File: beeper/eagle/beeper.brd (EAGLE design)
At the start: 29.2 x 39.8 mm, 30 parts, among them J4 ICSP, T1 MMBT3904, U1 ATA6631, U2 ATMEGA328P, X1 16MHz

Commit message: More beeper library cleanup.
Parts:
- C4: device rcl:C0805 -> beeper:C0805
- R3: device rcl:R0805 -> beeper:R0805
- T1: device transistor:SOT23-BEC -> beeper:SOT23-BEC
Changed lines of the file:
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@@
 <attribute name="NAME" x="25.4" y="26.4922" size="1.016" layer="25" ratio="10" rot="R270"/>
 </element>
-<element name="R3" library="rcl" package="R0805" value="3.3K" x="18.6182" y="13.5636" smashed="yes" rot="R180">
+<element name="R3" library="beeper" package="R0805" value="3.3K" x="18.6182" y="13.5636" smashed="yes" rot="R180">
 <attribute name="NAME" x="16.7894" y="13.208" size="1.016" layer="25" rot="R180"/>
 </element>
-<element name="T1" library="transistor" package="SOT23-BEC" value="MMBT3904" x="16.383" y="6.7564" smashed="yes" rot="R90">
+<element name="T1" library="beeper" package="SOT23-BEC" value="MMBT3904" x="16.383" y="6.7564" smashed="yes" rot="R90">
 <attribute name="NAME" x="14.8336" y="8.2804" size="1.016" layer="25" rot="R180"/>
 </element>
@@
 <attribute name="NAME" x="11.6238" y="14.1028" size="1.016" layer="25" rot="R90"/>
 </element>
-<element name="C4" library="rcl" package="C0805" value="0.1uF" x="14.8082" y="21.2344" smashed="yes" rot="R270">
+<element name="C4" library="beeper" package="C0805" value="0.1uF" x="14.8082" y="21.2344" smashed="yes" rot="R270">
 <attribute name="NAME" x="12.8524" y="21.4884" size="1.016" layer="25" rot="R270"/>
 </element>

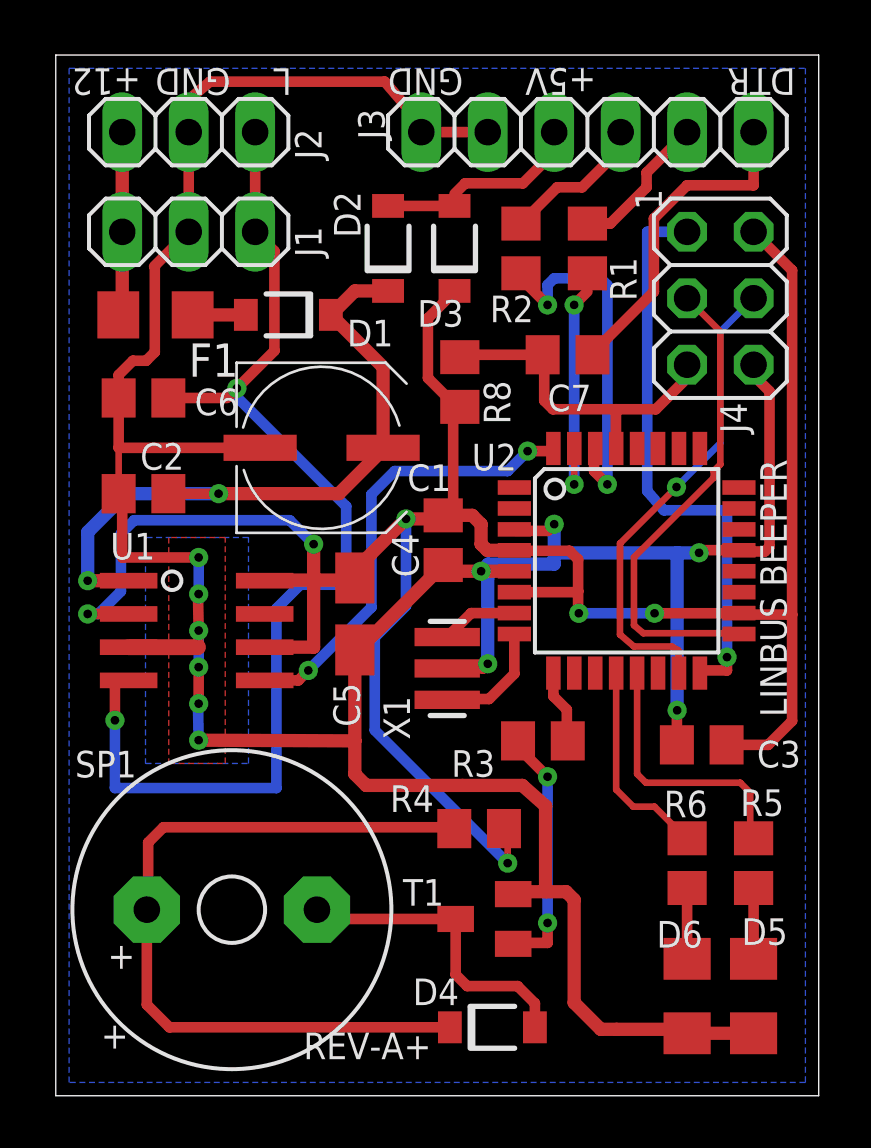
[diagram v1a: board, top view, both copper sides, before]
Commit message: Updated beeper board and schematic for Rev B.
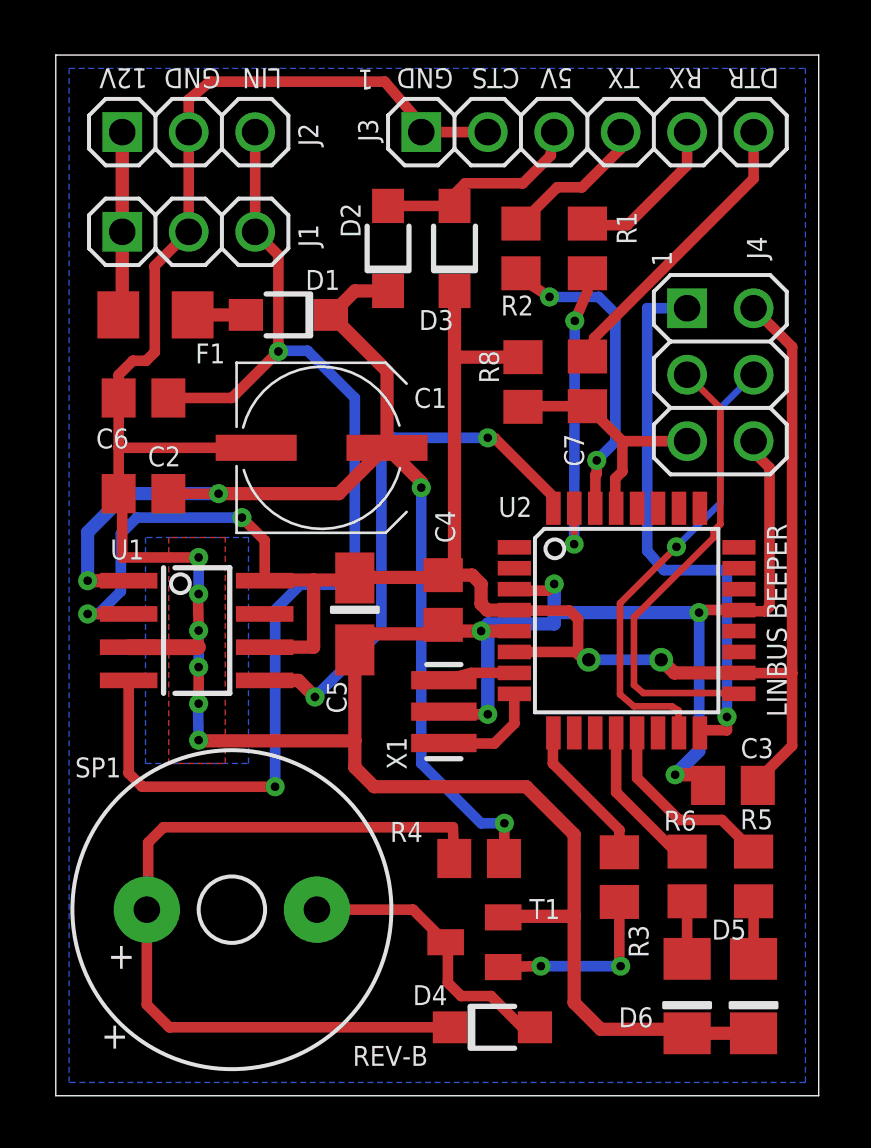
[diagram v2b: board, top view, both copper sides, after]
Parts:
- D5, D6: device beeper:1206 -> beeper:1206-LED
- R1, R2, R8: value 10k -> 10K
- R3, R5, R6: value 3.3K -> 3K3
- R4: value 0 -> 200R
- moved R3 5.97 mm to (21.5, 8.36), turned to 270 degrees
- moved J4 2.92 mm to (25.4, 27.6)
- moved R8 2.41 mm to (17.9, 27.3), turned to 90 degrees
- moved C4 2.29 mm to (14.8, 18.9)
- moved U2 2.29 mm to (21.8, 18.2)
- moved C3 1.96 mm to (25.9, 11.9)
- moved X1 1.66 mm to (14.8, 14.7)
- moved C7 1.27 mm to (20.3, 27.3), turned to 270 degrees
- moved R4 1.14 mm to (16.2, 9.07)
- moved T1 0.97 mm to (16.0, 5.87)
- moved R5 0.51 mm to (26.7, 8.38)
- moved R6 0.51 mm to (24.1, 8.38)
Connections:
- net +12V: now also R4.2
- net +5V: no longer R4.2
- net DTR: now also J3.6; no longer J3.1
- net GND: now also D5.C, D6.C, J3.1, J3.2; no longer D5.2, D6.2, J3.5, J3.6
- net N$3: now also D6.A; no longer D6.1
- net N$4: now also D5.A; no longer D5.1
- net RXI: now also J3.5; no longer J3.2
- net S-5V: now also J3.3; no longer J3.4
- net TXO: now also J3.4; no longer J3.3
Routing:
- net +5V: track 97.4 -> 77.8 mm, vias 6 -> 4
- net +12V: track 26.5 -> 44.7 mm, vias 2 -> 4
- net LIN_RX: track 17.2 -> 20.8 mm
- net RESET: track 13.1 -> 9.54 mm
- net ERROR_LED: track 10.3 -> 7.34 mm
- net BUZZER: track 2.82 -> 5.62 mm
- net N$19: track 9.52 -> 6.96 mm
- net SER_TX: track 9.65 -> 11.8 mm
- net FRAME_LED: track 7.93 -> 5.92 mm
- net SER_RX: track 14.1 -> 12.1 mm
- net DTR: track 12.5 -> 11.2 mm
- net N$30: track 30.1 -> 31.2 mm
- net N$31: track 12.0 -> 11.1 mm
- net XTAL2: track 4.94 -> 4.27 mm
- net MOSI: track 18.3 -> 17.7 mm
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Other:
- board text added: "12V"
- board text added: "5V"
- board text added: "CTS"
- board text added: "LIN"
- board text added: "REV-B"
- board text added: "RX"
- board text added: "TX"
- board text removed: "+12"
- board text removed: "+5V"
- board text removed: "L"
- board text removed: "REV-A+"

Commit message: Changed the beeper schematic to use the full atmega328p symbol. No Semantic change.
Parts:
- U2: value ATMEGA328P -> ATMEGA328
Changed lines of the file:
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@@
 <attribute name="NAME" x="10.8646" y="31.5628" size="0.762" layer="25" rot="R180"/>
 </element>
-<element name="U2" library="beeper" package="TQFP32-08" value="ATMEGA328P" x="21.8186" y="18.161" smashed="yes">
+<element name="U2" library="beeper" package="TQFP32-08" value="ATMEGA328" x="21.8186" y="18.161" smashed="yes">
 <attribute name="NAME" x="16.9164" y="22.1234" size="0.762" layer="25"/>
 </element>

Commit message: Completed the beeper schema cleanup. Added NC and debug signal ndicators.
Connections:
- net MISO renamed MISO/LIN_DATA
- net MOSI renamed MOSI/LIN_ERROR
- new net GP_DEBUG: U2.10
- new net LIN_BREAK: U2.23
- new net LIN_ISR: U2.26
- new net LIN_TICK: U2.1
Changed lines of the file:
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@@
 <wire x1="15.24" y1="34.4678" x2="15.24" y2="34.01" width="0.254" layer="1"/>
 </signal>
-<signal name="MOSI">
+<signal name="MOSI/LIN_ERROR">
 <contactref element="J4" pad="4"/>
 <contactref element="U2" pad="15"/>
@@
 <wire x1="25.4" y1="26.289" x2="26.67" y2="27.559" width="0.254" layer="16"/>
 </signal>
-<signal name="MISO">
+<signal name="MISO/LIN_DATA">
 <contactref element="J4" pad="1"/>
 <contactref element="U2" pad="16"/>
@@
 <signal name="N$1">
 </signal>
+<signal name="GP_DEBUG">
+<contactref element="U2" pad="10"/>
+</signal>
+<signal name="LIN_TICK">
+<contactref element="U2" pad="1"/>
+</signal>
+<signal name="LIN_BREAK">
+<contactref element="U2" pad="23"/>
+</signal>
+<signal name="LIN_ISR">
+<contactref element="U2" pad="26"/>
+</signal>
 </signals>

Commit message: Tweaked the layout. Should be ready for rev B.
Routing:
- net N$30: track 31.2 -> 30.6 mm
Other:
- board text added: "FEB/2014"
- board text added: "ICSP"
- board text added: "LINBUS BEEPER - REV B"
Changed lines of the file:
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@@
 <layer number="28" name="bValues" color="7" fill="1" visible="yes" active="yes"/>
 <layer number="29" name="tStop" color="7" fill="3" visible="no" active="yes"/>
-<layer number="30" name="bStop" color="7" fill="6" visible="no" active="yes"/>
+<layer number="30" name="bStop" color="7" fill="6" visible="yes" active="yes"/>
 <layer number="31" name="tCream" color="7" fill="4" visible="no" active="yes"/>
 <layer number="32" name="bCream" color="7" fill="5" visible="no" active="yes"/>
@@
 <wire x1="29.1592" y1="39.7764" x2="0" y2="39.7764" width="0" layer="20"/>
 <wire x1="0" y1="39.7764" x2="0" y2="0" width="0" layer="20"/>
-<text x="27.94" y="14.478" size="0.762" layer="21" rot="R90">LINBUS BEEPER</text>
-<text x="14.224" y="1.905" size="0.762" layer="21" rot="R180">REV-B</text>
+<text x="28.194" y="13.843" size="0.762" layer="21" rot="R90">LINBUS BEEPER</text>
+<text x="14.351" y="1.651" size="0.762" layer="21" rot="R180">REV-B</text>
 <text x="3.5052" y="39.2684" size="0.762" layer="21" rot="SR180">12V</text>
 <text x="6.2992" y="39.2684" size="0.762" layer="21" rot="SR180">GND</text>
@@
 <text x="15.1892" y="39.2684" size="0.762" layer="21" rot="SR180">GND</text>
 <text x="19.7612" y="39.2684" size="0.762" layer="21" rot="SR180">5V</text>
-<text x="23.5458" y="31.6992" size="0.762" layer="21" rot="SR90">1</text>
+<text x="23.7998" y="31.8262" size="0.762" layer="21" rot="SR90">1</text>
 <text x="27.6352" y="39.2684" size="0.762" layer="21" rot="SR180">DTR</text>
 <text x="1.7272" y="1.8034" size="1.016" layer="21" rot="SR0">+</text>
@@
 <text x="22.3012" y="39.2684" size="0.762" layer="21" rot="SR180">TX</text>
 <text x="17.7292" y="39.2684" size="0.762" layer="21" rot="SR180">CTS</text>
-<text x="12.1412" y="39.2176" size="0.762" layer="21" rot="SR180">1</text>
+<text x="12.5222" y="35.9156" size="0.762" layer="21" rot="SR180">1</text>
+<text x="27.94" y="2.159" size="1.016" layer="30" font="vector" ratio="15" rot="MR180" align="bottom-right">LINBUS BEEPER - REV B</text>
+<text x="25.527" y="31.877" size="0.762" layer="21" rot="R90">ICSP</text>
+<text x="16.637" y="11.43" size="0.762" layer="21">FEB/2014</text>
 </plain>
 <attributes>
@@
 <param name="mlMinCreamFrame" value="0mil"/>
 <param name="mlMaxCreamFrame" value="0mil"/>
-<param name="mlViaStopLimit" value="13mil"/>
+<param name="mlViaStopLimit" value="20mil"/>
 <param name="srRoundness" value="0"/>
 <param name="srMinRoundness" value="0mil"/>
@@
 </element>
 <element name="J1" library="beeper" package="1X03" value="" x="5.08" y="33.02" smashed="yes">
-<attribute name="NAME" x="10.033" y="32.4358" size="0.762" layer="25" ratio="10" rot="R90"/>
+<attribute name="NAME" x="10.16" y="33.4518" size="0.762" layer="25" ratio="10" rot="SR180"/>
 <attribute name="VALUE" x="1.27" y="29.845" size="1.27" layer="27"/>
 </element>
 <element name="C3" library="beeper" package="C0805" value="0.1uF" x="25.8826" y="11.8618" smashed="yes" rot="R180">
-<attribute name="NAME" x="27.432" y="13.6652" size="0.762" layer="25" rot="R180"/>
+<attribute name="NAME" x="26.543" y="13.5382" size="0.762" layer="25" rot="R180"/>
 </element>
 <element name="C7" library="beeper" package="C0805" value="0.1uF" x="20.32" y="27.305" smashed="yes" rot="R270">
-<attribute name="NAME" x="19.431" y="25.2984" size="0.762" layer="25" rot="R270"/>
+<attribute name="NAME" x="21.336" y="27.8384" size="0.762" layer="25" rot="R270"/>
 </element>
 <element name="R1" library="beeper" package="R0805" value="10K" x="20.32" y="32.385" smashed="yes" rot="R90">
@@
 </element>
 <element name="J4" library="beeper" package="2X03" value="ICSP" x="25.4" y="27.559" smashed="yes" rot="R270">
-<attribute name="NAME" x="26.416" y="32.8422" size="0.762" layer="25" ratio="10" rot="R270"/>
+<attribute name="NAME" x="27.051" y="31.9532" size="0.762" layer="25" ratio="10" rot="R90"/>
 </element>
 <element name="R3" library="beeper" package="R0805" value="3K3" x="21.5392" y="8.3566" smashed="yes" rot="R270">
-<attribute name="NAME" x="21.8948" y="6.5278" size="0.762" layer="25" rot="R270"/>
+<attribute name="NAME" x="19.2278" y="8.6868" size="0.762" layer="25"/>
 </element>
 <element name="T1" library="beeper" package="SOT23-BEC" value="MMBT3904" x="16.002" y="5.8674" smashed="yes" rot="R90">
-<attribute name="NAME" x="19.2786" y="7.5184" size="0.762" layer="25" rot="R180"/>
+<attribute name="NAME" x="19.2786" y="6.5024" size="0.762" layer="25" rot="R180"/>
 </element>
 <element name="R4" library="beeper" package="R0805" value="200R" x="16.1798" y="9.0678" smashed="yes">
-<attribute name="NAME" x="12.7762" y="9.7028" size="0.762" layer="25"/>
+<attribute name="NAME" x="14.8082" y="10.2108" size="0.762" layer="25"/>
 </element>
 <element name="R8" library="beeper" package="R0805" value="10K" x="17.8562" y="27.2796" smashed="yes" rot="R90">
-<attribute name="NAME" x="16.9418" y="27.2288" size="0.762" layer="25" rot="R90"/>
+<attribute name="NAME" x="16.8148" y="26.4668" size="0.762" layer="25" rot="R90"/>
 </element>
 <element name="U1" library="beeper" package="SO-08" value="ATA6631" x="5.3848" y="17.78" smashed="yes" rot="R270">
@@
 </element>
 <element name="J3" library="beeper" package="1X06" value="" x="20.32" y="36.83" smashed="yes" rot="R180">
-<attribute name="NAME" x="11.557" y="37.338" size="0.762" layer="25" ratio="10" rot="R270"/>
+<attribute name="NAME" x="12.319" y="37.211" size="0.762" layer="25" ratio="10" rot="SR180"/>
 <attribute name="VALUE" x="27.94" y="40.005" size="1.27" layer="27" rot="R180"/>
 </element>
 <element name="J2" library="beeper" package="1X03" value="" x="5.08" y="36.83" smashed="yes">
-<attribute name="NAME" x="10.033" y="36.2966" size="0.762" layer="25" ratio="10" rot="R90"/>
+<attribute name="NAME" x="10.287" y="37.1856" size="0.762" layer="25" ratio="10" rot="SR180"/>
 <attribute name="VALUE" x="1.27" y="33.655" size="1.27" layer="27"/>
 </element>
 <element name="D1" library="beeper" package="SOD123FL" value="MBR0540" x="8.89" y="29.845" smashed="yes" rot="R180">
-<attribute name="NAME" x="10.8646" y="31.5628" size="0.762" layer="25" rot="R180"/>
+<attribute name="NAME" x="10.3566" y="31.6898" size="0.762" layer="25" rot="R180"/>
 </element>
 <element name="U2" library="beeper" package="TQFP32-08" value="ATMEGA328" x="21.8186" y="18.161" smashed="yes">
@@
 </element>
 <element name="D3" library="beeper" package="SOD123FL" value="MBR0540" x="15.24" y="32.385" smashed="yes" rot="R90">
-<attribute name="NAME" x="15.2052" y="30.0294" size="0.762" layer="25" rot="R180"/>
+<attribute name="NAME" x="15.3322" y="29.9024" size="0.762" layer="25" rot="R180"/>
 </element>
 <element name="X1" library="beeper" package="RESONATOR-SMD" value="16MHz" x="14.8336" y="14.6812" smashed="yes" rot="R90">
-<attribute name="NAME" x="13.4112" y="12.4714" size="0.762" layer="25" rot="R90"/>
+<attribute name="NAME" x="13.2842" y="13.4874" size="0.762" layer="25" rot="R90"/>
 </element>
 <element name="SP1" library="beeper" package="AL60P" value="WT-1205" x="6.731" y="7.112" smashed="yes">
@@
 </element>
 <element name="D5" library="beeper" package="1206-LED" value="RED" x="26.67" y="3.81" smashed="yes" rot="R270">
-<attribute name="NAME" x="25.0698" y="5.969" size="0.762" layer="25"/>
+<attribute name="NAME" x="26.0858" y="0.635" size="0.762" layer="25"/>
 </element>
 <element name="D6" library="beeper" package="1206-LED" value="GREEN" x="24.13" y="3.81" smashed="yes" rot="R270">
@@
 <wire x1="4.3434" y1="2.6162" x2="3.4798" y2="3.4798" width="0.4064" layer="1"/>
 <wire x1="3.4798" y1="3.4798" x2="3.4798" y2="7.112" width="0.4064" layer="1"/>
-<wire x1="15.2298" y1="9.0678" x2="15.179" y2="10.2616" width="0.4064" layer="1"/>
-<wire x1="15.179" y1="10.2616" x2="4.1148" y2="10.2616" width="0.4064" layer="1"/>
 <wire x1="4.1148" y1="10.2616" x2="3.5306" y2="9.6774" width="0.4064" layer="1"/>
 <wire x1="3.5306" y1="9.6774" x2="3.5306" y2="7.1628" width="0.4064" layer="1"/>
 <wire x1="3.5306" y1="7.1628" x2="3.4798" y2="7.112" width="0.4064" layer="1"/>
+<wire x1="4.1148" y1="10.2616" x2="14.036" y2="10.2616" width="0.4064" layer="1"/>
+<wire x1="14.036" y1="10.2616" x2="15.2298" y2="9.0678" width="0.4064" layer="1"/>
 </signal>
 <signal name="XTAL1">
